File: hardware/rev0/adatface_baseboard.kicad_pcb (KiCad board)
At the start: 4 copper layers, 121.3 x 111.6 mm, 92 parts, among them J1 Conn_01x06_Male, J10 - GND Conn_01x04_Male, J11 - GND Conn_01x04_Male, J2 Conn_02x32_Odd_Even, J3 Conn_02x32_Odd_Even, J4 Connector_USB_C_Receptacle_US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, J5 Connector_USB_C_Receptacle_US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, J6 Conn_01x06_Male, J7 Conn_01x26_Male, J8 Conn_01x01_Male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

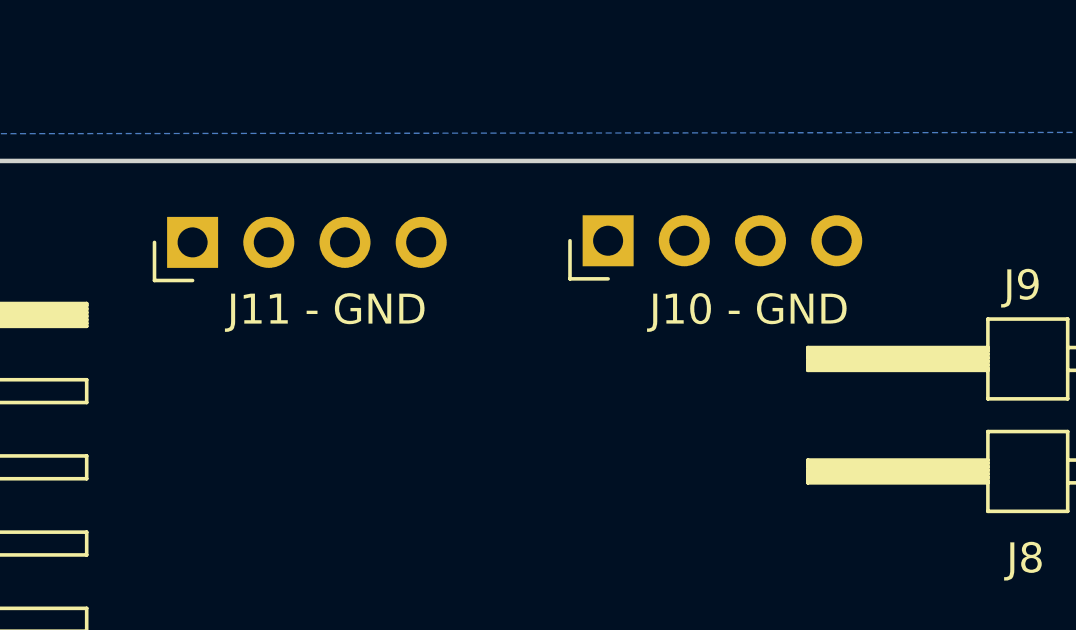
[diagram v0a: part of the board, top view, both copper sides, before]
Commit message: fix reference designators on GND headers
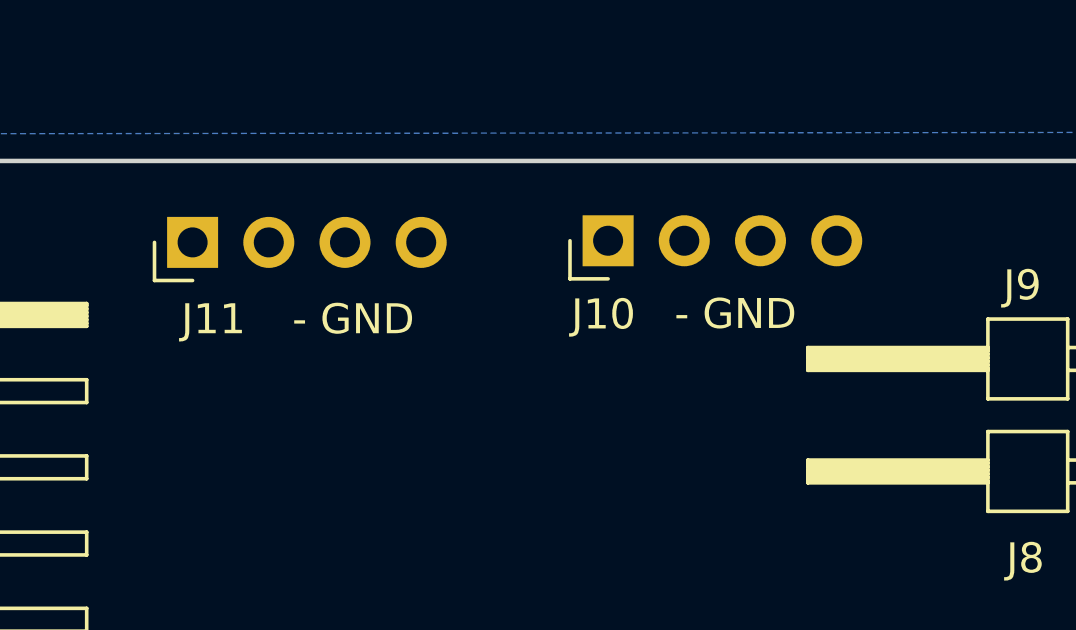
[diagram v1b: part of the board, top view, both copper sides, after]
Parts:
- J10: renamed from J10 - GND
- J11: renamed from J11 - GND
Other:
- board text added: "- GND"
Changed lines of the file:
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@@
     (property "Sheetname" "")
     (attr through_hole)
-    (fp_text reference "J11 - GND" (at -2.245 4.48 180) (layer "F.SilkS")
-      (effects (font (size 1 1) (thickness 0.15)))
+    (fp_text reference "J11" (at -2.565 -0.38 180) (layer "F.SilkS")
+      (effects (font (size 1 1) (thickness 0.15)) (justify left))
     )
     (fp_text value "Conn_01x04_Male" (at 4.385 9.89 90) (layer "F.Fab") hide
@@
     (property "Sheetname" "")
     (attr through_hole)
-    (fp_text reference "J10 - GND" (at -2.3 4.7 180) (layer "F.SilkS")
+    (fp_text reference "J10" (at -2.46 -0.155 180) (layer "F.SilkS")
       (effects (font (size 1 1) (thickness 0.15)))
     )
@@
     (effects (font (size 2 2) (thickness 0.3)))
   )
+  (gr_text " - GND" (at 98.78 41.93) (layer "F.SilkS")
+    (effects (font (size 1 1) (thickness 0.15)))
+  )
   (gr_text "RX" (at 44.488096 112) (layer "F.SilkS")
     (effects (font (size 2 2) (thickness 0.3)))
@@
     (effects (font (size 2 2) (thickness 0.3)))
   )
+  (gr_text " - GND" (at 111.52 41.755) (layer "F.SilkS")
+    (effects (font (size 1 1) (thickness 0.15)))
+  )
   (gr_text "ADAT2" (at 47.25 105.25) (layer "F.SilkS")

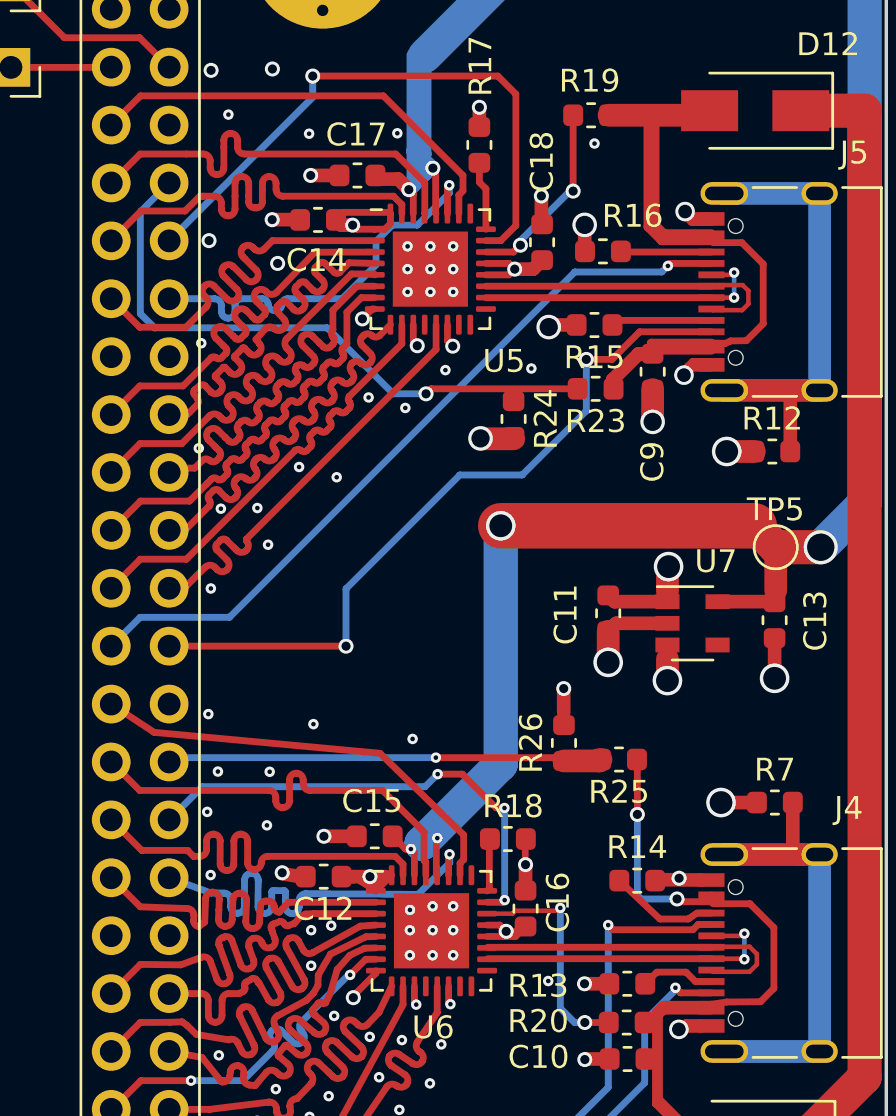
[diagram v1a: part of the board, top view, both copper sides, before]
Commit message: length and 90Ohm impedence match D- and D+
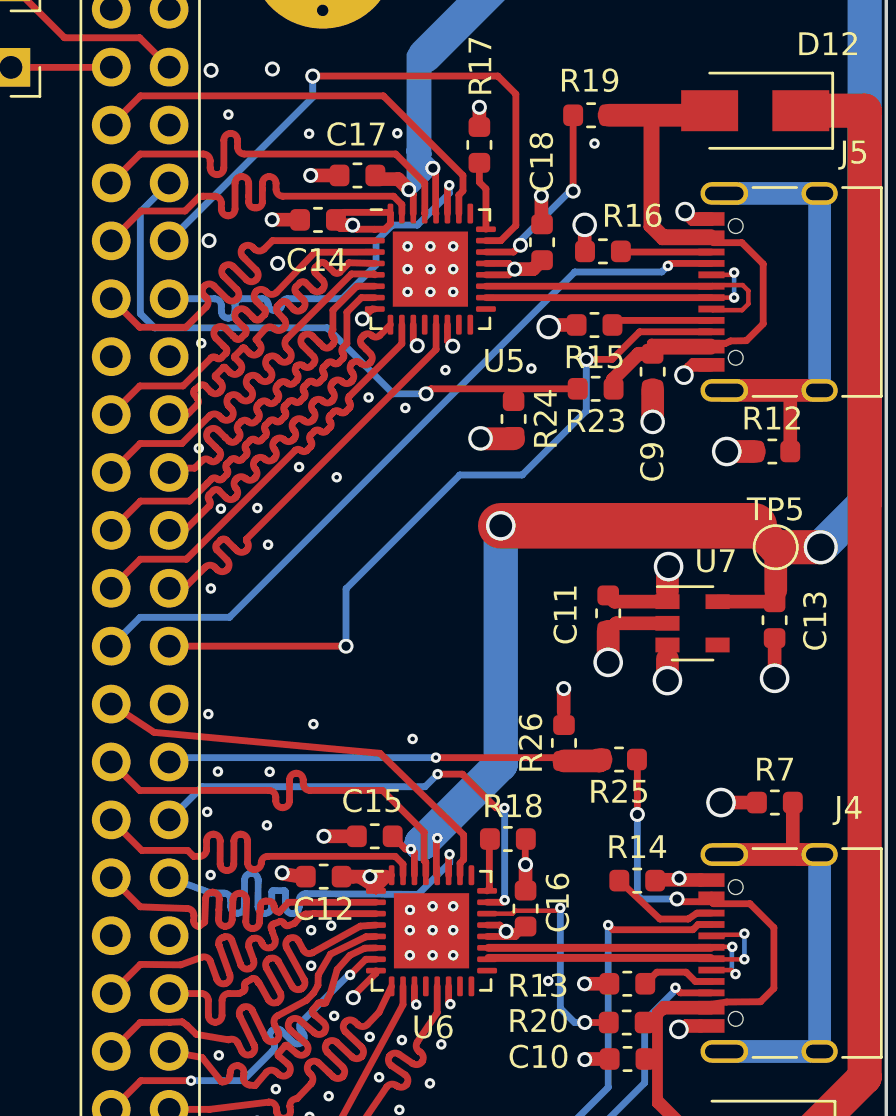
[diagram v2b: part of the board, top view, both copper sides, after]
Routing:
- net /USB1_D-: track 14.6 -> 13.1 mm, vias 0 -> 2
- net /USB1_D+: track 12.8 -> 13.7 mm
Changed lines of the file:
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@@
   (segment (start 142.03 81.29) (end 141.795263 81.29) (width 0.3) (layer "B.Cu") (net 8))
   (segment (start 142.26 81.06) (end 142.03 81.29) (width 0.3) (layer "B.Cu") (net 8))
-  (segment (start 141.9 51.25) (end 141.9 50.66) (width 0.6) (layer "B.Cu") (net 8))
+  (segment (start 141.9 52.16925) (end 141.9 50.66) (width 0.6) (layer "B.Cu") (net 8))
   (segment (start 141.705105 52.364145) (end 142.4 51.66925) (width 0.6) (layer "B.Cu") (net 8))
   (segment (start 142.225 50.985) (end 142.325 50.985) (width 0.6) (layer "B.Cu") (net 8))
   (segment (start 141.795263 81.29) (end 141.8 81.285263) (width 0.3) (layer "B.Cu") (net 8))
-  (segment (start 141.9 52.16925) (end 141.9 51.25) (width 0.6) (layer "B.Cu") (net 8))
   (segment (start 142.025263 81.06) (end 141.795263 81.29) (width 0.3) (layer "B.Cu") (net 8))
   (segment (start 142.325 50.985) (end 142.76 51.42) (width 0.6) (layer "B.Cu") (net 8))
@@
   (segment (start 144.0795 52.418529) (end 143.9 52.598029) (width 0.3) (layer "F.Cu") (net 44))
   (segment (start 142.405105 52.074195) (end 141.13091 50.8) (width 0.3) (layer "F.Cu") (net 45))
-  (segment (start 131.946434 50.8) (end 129.92 50.8) (width 0.3) (layer "F.Cu") (net 45))
-  (segment (start 133.59 50.5) (end 133.59 51.406324) (width 0.3) (layer "F.Cu") (net 45))
+  (segment (start 129.92 50.8) (end 132.69 50.8) (width 0.3) (layer "F.Cu") (net 45))
+  (segment (start 133.59 50.193676) (end 133.59 51.406324) (width 0.3) (layer "F.Cu") (net 45))
   (segment (start 132.99 51.406324) (end 132.99 51.1) (width 0.3) (layer "F.Cu") (net 45))
   (segment (start 134.19 50.5) (end 134.19 50.193676) (width 0.3) (layer "F.Cu") (net 45))
@@
   (segment (start 129.92 50.8) (end 128.65 52.07) (width 0.3) (layer "F.Cu") (net 45))
   (segment (start 142.4 53.4125) (end 142.405105 53.407395) (width 0.3) (layer "F.Cu") (net 45))
-  (segment (start 132.69 50.8) (end 131.946434 50.8) (width 0.3) (layer "F.Cu") (net 45))
-  (segment (start 133.59 50.193676) (end 133.59 50.5) (width 0.3) (layer "F.Cu") (net 45))
   (arc (start 132.99 51.1) (mid 132.902132 50.887868) (end 132.69 50.8) (width 0.3) (layer "F.Cu") (net 45))
   (arc (start 134.49 50.8) (mid 134.277868 50.712132) (end 134.19 50.5) (width 0.3) (layer "F.Cu") (net 45))
@@
   (segment (start 133.48 53.212043) (end 133.48 52.95) (width 0.3) (layer "F.Cu") (net 47))
   (segment (start 141.4 53.02) (end 141.03 52.65) (width 0.3) (layer "F.Cu") (net 47))
-  (segment (start 134.08 52.65) (end 134.08 53.212043) (width 0.3) (layer "F.Cu") (net 47))
+  (segment (start 134.08 52.087957) (end 134.08 53.212043) (width 0.3) (layer "F.Cu") (net 47))
   (segment (start 141.4 53.4125) (end 141.4 53.02) (width 0.3) (layer "F.Cu") (net 47))
   (segment (start 129.96 53.3) (end 128.65 54.61) (width 0.3) (layer "F.Cu") (net 47))
-  (segment (start 134.08 52.087957) (end 134.08 52.65) (width 0.3) (layer "F.Cu") (net 47))
   (segment (start 135.88 52.35) (end 135.88 52.087957) (width 0.3) (layer "F.Cu") (net 47))
   (segment (start 131.89 53.3) (end 129.96 53.3) (width 0.3) (layer "F.Cu") (net 47))
@@
   (segment (start 154.98 87.1) (end 154.2772 87.1) (width 0.3) (layer "F.Cu") (net 113))
   (segment (start 154.2772 87.1) (end 153.8672 86.69) (width 0.3) (layer "F.Cu") (net 113))
-  (segment (start 156.425 86.125) (end 156.4 86.1) (width 0.2) (layer "F.Cu") (net 114))
-  (segment (start 156.4 86.1) (end 155.505 86.1) (width 0.2) (layer "F.Cu") (net 114))
-  (segment (start 156.425 85) (end 156.325 85.1) (width 0.2) (layer "F.Cu") (net 114))
-  (segment (start 154.98 86.1) (end 145.1625 86.1) (width 0.3) (layer "F.Cu") (net 114))
-  (segment (start 156.325 85.1) (end 155.505 85.1) (width 0.2) (layer "F.Cu") (net 114))
+  (segment (start 156.4205 86.1295) (end 155.0095 86.1295) (width 0.2) (layer "F.Cu") (net 114))
+  (segment (start 156.385 85.05) (end 155.565 85.05) (width 0.2) (layer "F.Cu") (net 114))
+  (segment (start 155.505 85.1) (end 154.98 85.1) (width 0.2) (layer "F.Cu") (net 114))
+  (segment (start 156.425 86.125) (end 156.4205 86.1295) (width 0.2) (layer "F.Cu") (net 114))
+  (segment (start 145.1975 86.065) (end 154.945 86.065) (width 0.35) (layer "F.Cu") (net 114))
+  (segment (start 156.425 85) (end 156.4005 85.0245) (width 0.2) (layer "F.Cu") (net 114))
+  (via (at 156.425 85) (size 0.46) (drill 0.2) (layers "F.Cu" "B.Cu") (net 114))
   (via (at 156.425 86.125) (size 0.46) (drill 0.2) (layers "F.Cu" "B.Cu") (net 114))
-  (via (at 156.425 85) (size 0.46) (drill 0.2) (layers "F.Cu" "B.Cu") (net 114))
   (segment (start 156.425 85) (end 156.425 86.125) (width 0.2) (layer "B.Cu") (net 114))
-  (segment (start 154.98 85.6) (end 145.1625 85.6) (width 0.3) (layer "F.Cu") (net 115))
-  (segment (start 156.975 86.352818) (end 156.975 85.897182) (width 0.2) (layer "F.Cu") (net 115))
-  (segment (start 156.652818 85.575) (end 155.005 85.575) (width 0.2) (layer "F.Cu") (net 115))
   (segment (start 155.005 85.575) (end 154.98 85.6) (width 0.2) (layer "F.Cu") (net 115))
-  (segment (start 156.975 85.897182) (end 156.652818 85.575) (width 0.2) (layer "F.Cu") (net 115))
-  (segment (start 156.652818 86.675) (end 156.975 86.352818) (width 0.2) (layer "F.Cu") (net 115))
-  (segment (start 154.98 86.6) (end 155.055 86.675) (width 0.2) (layer "F.Cu") (net 115))
-  (segment (start 155.055 86.675) (end 156.652818 86.675) (width 0.2) (layer "F.Cu") (net 115))
+  (segment (start 145.1875 85.625) (end 154.955 85.625) (width 0.35) (layer "F.Cu") (net 115))
+  (segment (start 155.86 86.6) (end 154.98 86.6) (width 0.2) (layer "F.Cu") (net 115))
+  (segment (start 155.0005 85.5795) (end 154.98 85.6) (width 0.2) (layer "F.Cu") (net 115))
+  (segment (start 156.035 86.775) (end 155.86 86.6) (width 0.2) (layer "F.Cu") (net 115))
+  (segment (start 155.8955 85.5795) (end 155.0005 85.5795) (width 0.2) (layer "F.Cu") (net 115))
+  (via (at 155.8955 85.5795) (size 0.46) (drill 0.2) (layers "F.Cu" "B.Cu") (net 115))
+  (via (at 156.035 86.775) (size 0.46) (drill 0.2) (layers "F.Cu" "B.Cu") (net 115))
+  (segment (start 155.875 85.6) (end 155.875 86.615) (width 0.2) (layer "B.Cu") (net 115))
+  (segment (start 155.875 86.615) (end 156.035 86.775) (width 0.2) (layer "B.Cu") (net 115))
+  (segment (start 155.8955 85.5795) (end 155.875 85.6) (width 0.2) (layer "B.Cu") (net 115))
   (segment (start 152.72 84.36) (end 150.9375 82.675) (width 0.3) (layer "F.Cu") (net 116))
   (segment (start 154.98 84.1) (end 154.346112 84.1) (width 0.3) (layer "F.Cu") (net 116))

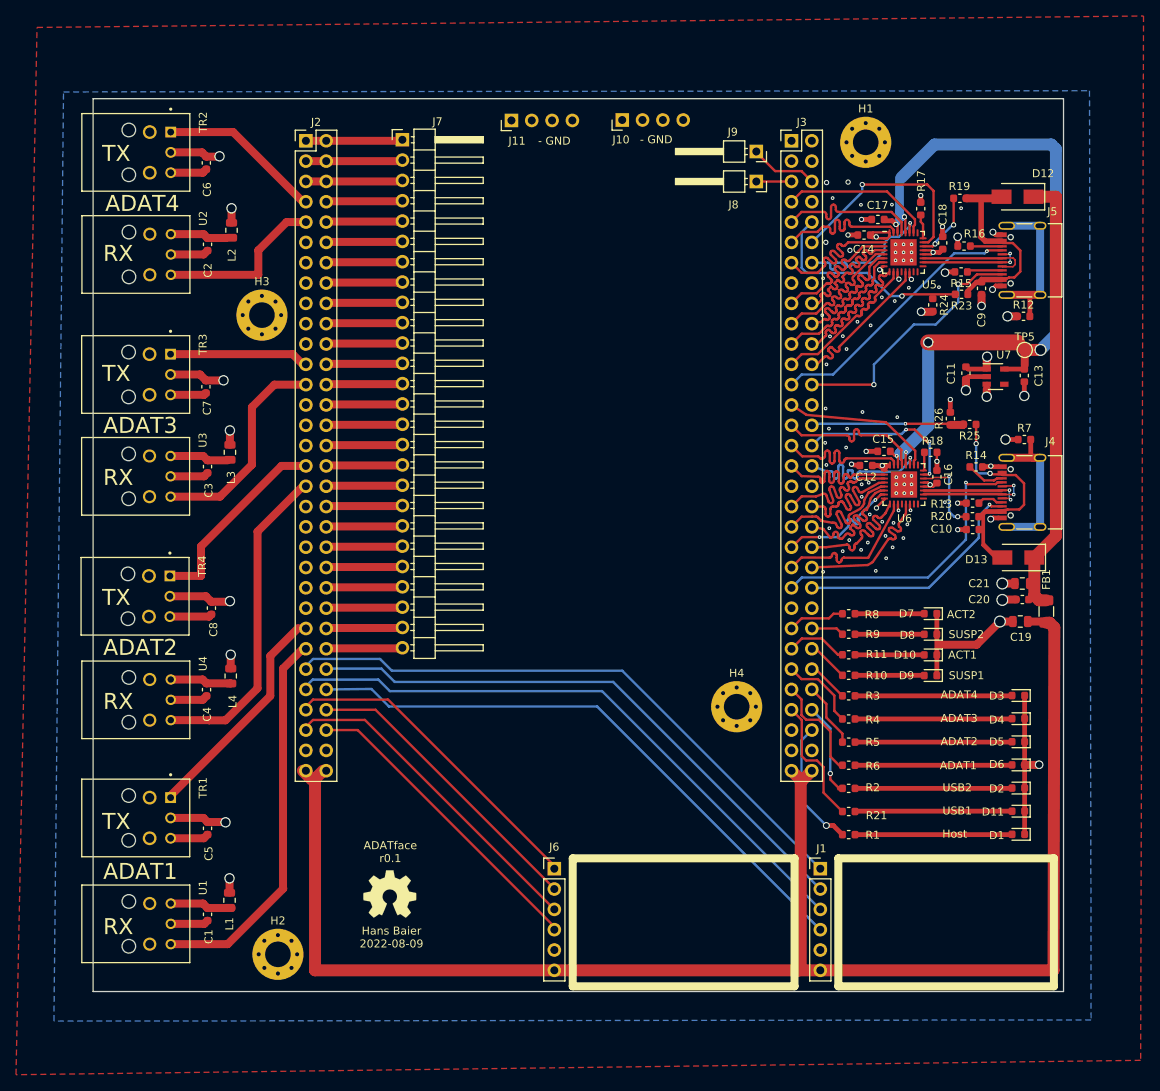
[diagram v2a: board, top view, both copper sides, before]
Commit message: Add nikitalita to the credits on the board. Also adjust diff pair of the top PHY
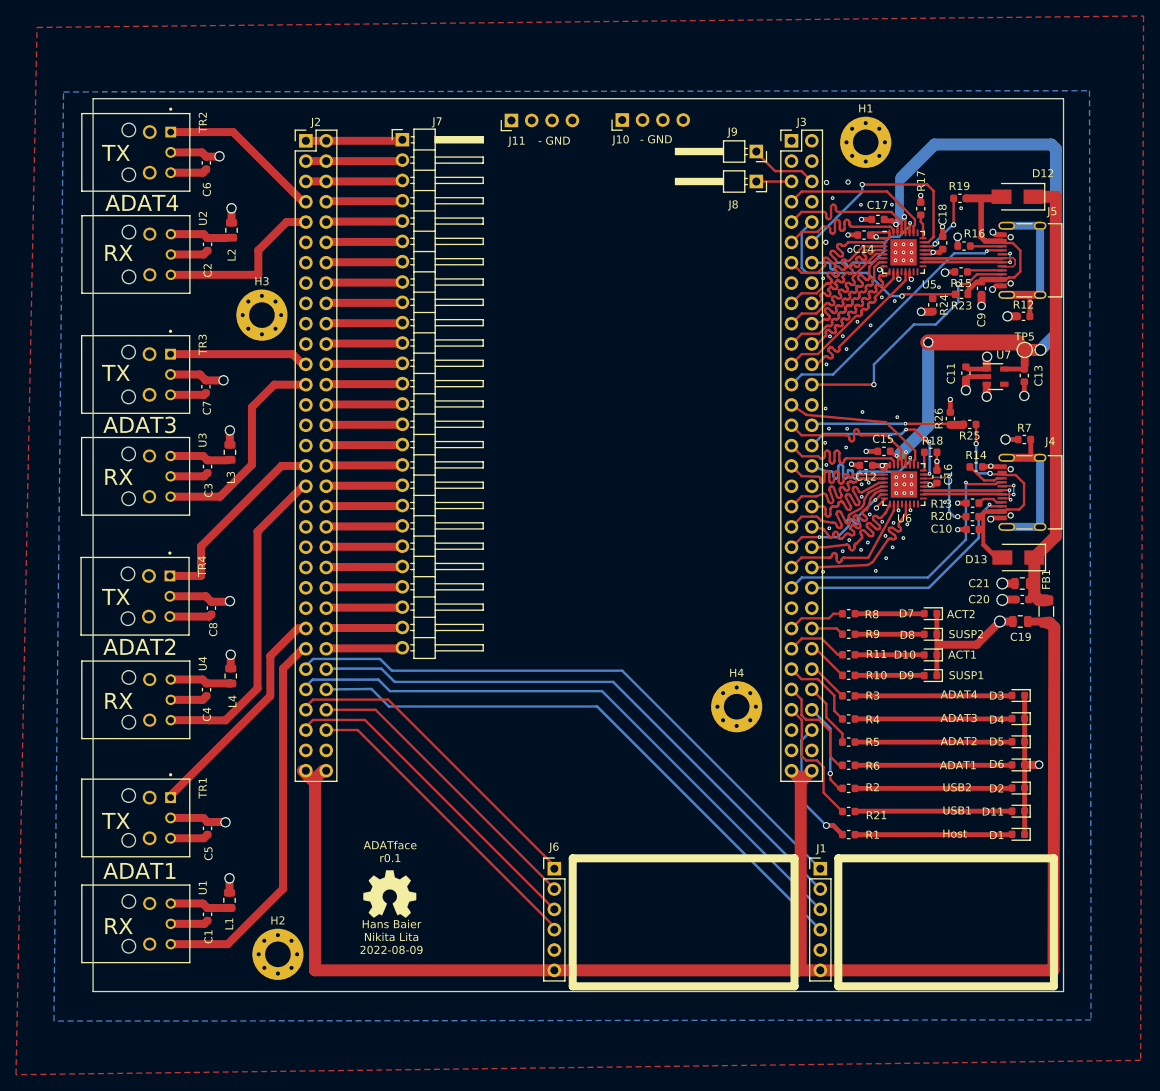
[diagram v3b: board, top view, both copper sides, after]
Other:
- board text added: "Hans Baier Nikita Lita 2022-08-09"
- board text removed: "Hans Baier 2022-08-09"
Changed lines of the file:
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@@
   (gr_rect (start 101.3 131.6) (end 129.025 147.6) (layer "F.SilkS") (width 1) (fill none))
   (gr_rect (start 41.35 36.65) (end 162.65 148.25) (layer "Edge.Cuts") (width 0.15) (fill none))
-  (gr_text "Hans Baier\n2022-08-09" (at 78.65 141.475) (layer "F.SilkS")
+  (gr_text "Hans Baier\nNikita Lita\n2022-08-09" (at 78.65 141.475) (layer "F.SilkS")
     (effects (font (size 1 1) (thickness 0.15)))
   )
@@
   (segment (start 148.975 88.9) (end 149.425 88.9) (width 0.3) (layer "B.Cu") (net 70))
   (segment (start 154.98 55.1) (end 151.0375 55.1) (width 0.3) (layer "F.Cu") (net 80))
-  (segment (start 145.0875 57.1) (end 154.98 57.1) (width 0.3) (layer "F.Cu") (net 81))
+  (segment (start 145.10375 57.06) (end 154.99625 57.06) (width 0.35) (layer "F.Cu") (net 81))
   (segment (start 155.975 56) (end 155.875 56.1) (width 0.2) (layer "F.Cu") (net 81))
   (segment (start 155.875 56.1) (end 154.98 56.1) (width 0.2) (layer "F.Cu") (net 81))
@@
   (segment (start 155.03 57.65) (end 156.325 57.65) (width 0.2) (layer "F.Cu") (net 82))
   (segment (start 156.6 57.375) (end 156.6 56.8) (width 0.2) (layer "F.Cu") (net 82))
-  (segment (start 145.0875 56.6) (end 154.98 56.6) (width 0.3) (layer "F.Cu") (net 82))
+  (segment (start 145.0875 56.62) (end 154.98 56.62) (width 0.35) (layer "F.Cu") (net 82))
   (segment (start 154.98 58.6) (end 151.83 58.6) (width 0.3) (layer "F.Cu") (net 83))
   (segment (start 150.62 59.81) (end 149.49 59.81) (width 0.3) (layer "F.Cu") (net 83))
